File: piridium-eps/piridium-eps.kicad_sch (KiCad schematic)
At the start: 15 parts

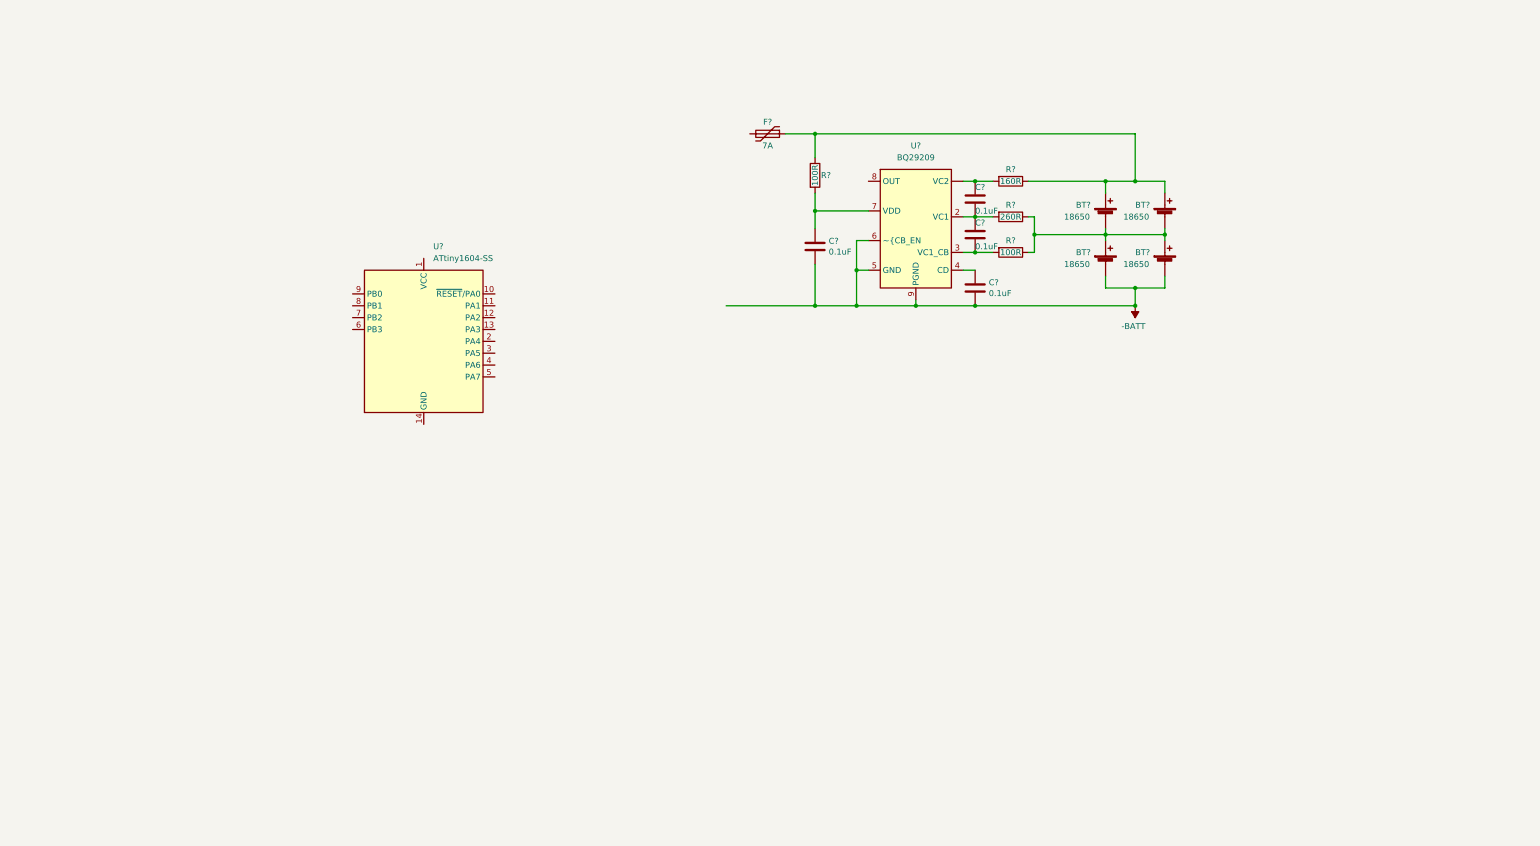
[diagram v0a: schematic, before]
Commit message: transfer some TJ-EPS circuitry to eps
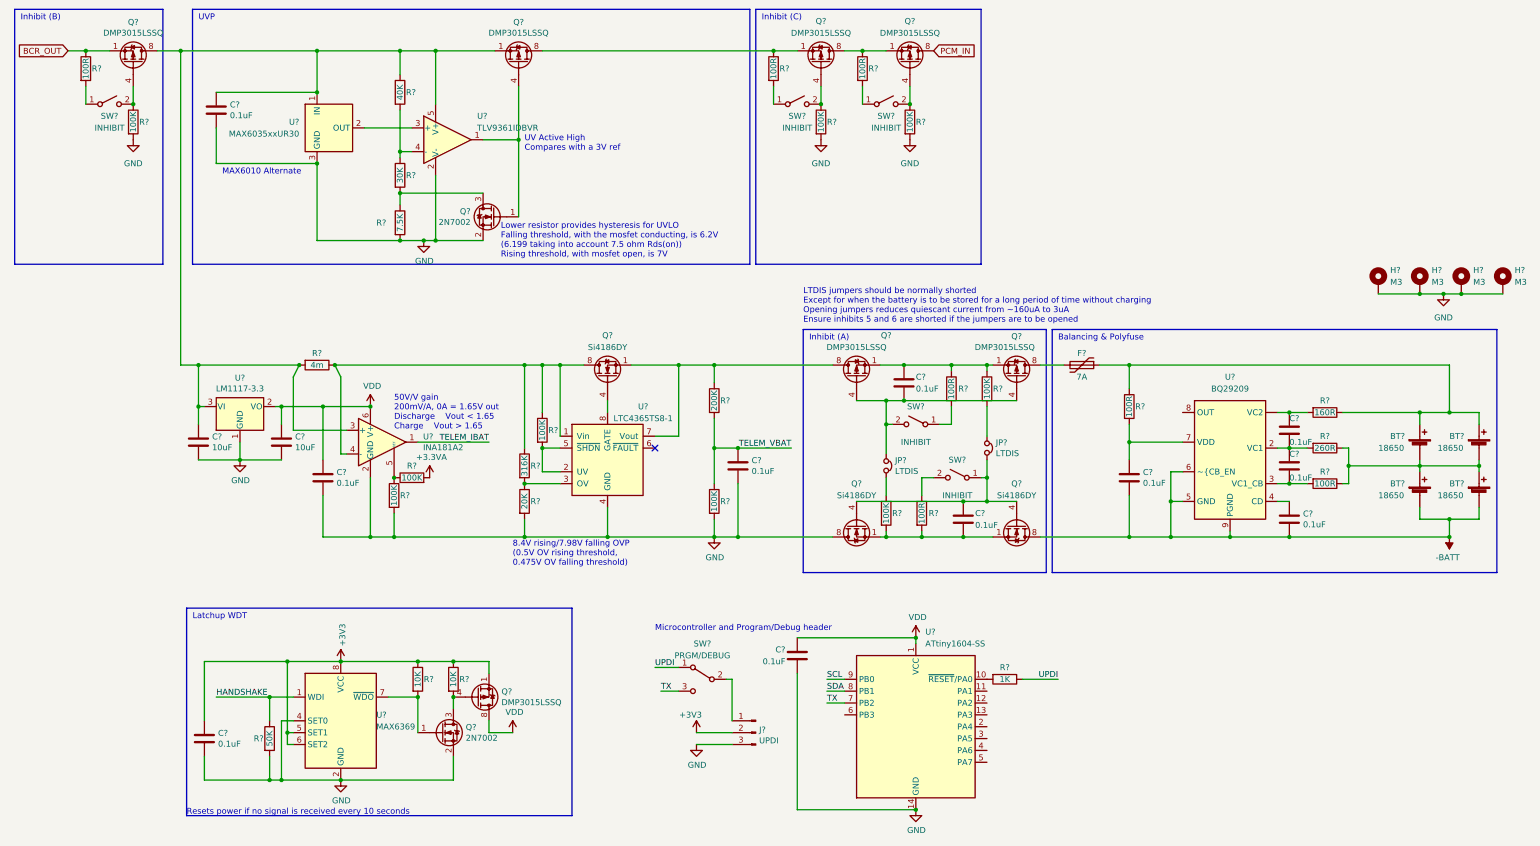
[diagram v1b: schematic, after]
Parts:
- added C? (x6): 0.1uF, Capacitor_SMD:C_0805_2012Metric, symbol Device:C
- added C? (x2): 10uF, Capacitor_SMD:C_0805_2012Metric, symbol Device:C
- added C?: 0.1uF, symbol Device:C
- added H? (x4): M3, MountingHole:MountingHole_3.2mm_M3_DIN965_Pad, symbol Mechanical:MountingHole_Pad
- added J?: UPDI, Connector_PinHeader_2.54mm:PinHeader_1x03_P2.54mm_Vertical, symbol Connector:Conn_01x03_Male
- added JP? (x2): LTDIS, Jumper:SolderJumper-2_P1.3mm_Open_Pad1.0x1.5mm, symbol BatteryMaster-rescue:Jumper_NC_Small-Device
- added Q? (x7): DMP3015LSSQ, Package_SO:SOIC-8_3.9x4.9mm_P1.27mm, symbol Transistor_FET:IRF7404
- added Q? (x2): 2N7002, Package_TO_SOT_SMD:SOT-23, symbol Transistor_FET:2N7002
- added Q? (x3): Si4186DY, Package_SO:SOIC-8_3.9x4.9mm_P1.27mm, symbol Transistor_FET:Si4162DY
- added R? (x9): 100K, Resistor_SMD:R_0805_2012Metric, symbol Device:R
- added R?: 1K, Resistor_SMD:R_1206_3216Metric, symbol Device:R
- added R? (x5): 100R, Resistor_SMD:R_0805_2012Metric, symbol Device:R
- added R?: 200K, Resistor_SMD:R_0805_2012Metric, symbol Device:R
- added R?: 30K, Resistor_SMD:R_0805_2012Metric, symbol Device:R
- added R? (x2): 10K, Resistor_SMD:R_0805_2012Metric, symbol Device:R
- added R?: 7.5K, Resistor_SMD:R_0805_2012Metric, symbol Device:R
- added R?: 4m, Resistor_SMD:R_1206_3216Metric, symbol Device:R
- added R?: 40K, Resistor_SMD:R_0805_2012Metric, symbol Device:R
- added R?: 316K, Resistor_SMD:R_0805_2012Metric, symbol Device:R
- added R?: 20K, Resistor_SMD:R_0805_2012Metric, symbol Device:R
- added R?: 50K, Resistor_SMD:R_0805_2012Metric, symbol Device:R
- added SW? (x5): INHIBIT, Connector_Hirose:Hirose_DF13-02P-1.25DSA_1x02_P1.25mm_Vertical, symbol Switch:SW_SPST
- added SW?: PRGM/DEBUG, Button_Switch_THT:SW_Slide_1P2T_CK_OS102011MS2Q, symbol Switch:SW_SPDT
- added U?: INA181A2, Package_TO_SOT_SMD:SOT-23-6, symbol Amplifier_Current:INA181
- added U?: MAX6369, Package_TO_SOT_SMD:SOT-23-8, symbol Power_Supervisor:MAX6369
- added U?: LM1117-3.3, Package_TO_SOT_SMD:SOT-223-3_TabPin2, symbol Regulator_Linear:LM1117-3.3
- added U?: LTC4365TS8-1, Package_TO_SOT_SMD:TSOT-23-8, symbol Power_Management:LTC4365TS8-1
- added U?: MAX6035xxUR30, Package_TO_SOT_SMD:SOT-23, symbol Reference_Voltage:MAX6035xxUR30
- added U?: TLV9361IDBVR, Package_TO_SOT_SMD:SOT-23-5, symbol Amplifier_Operational:OPA842xDBV
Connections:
- net -BATT: now also Q?.5 (D), Q?.6 (D), Q?.7 (D), Q?.8 (D)
- net at F?.2: now also Q?.5 (D), Q?.6 (D), Q?.7 (D), Q?.8 (D)
- net VDD: now reaches U?.1 (VCC)
- net VDD: now also C?.1, C?.1, C?.1, Q?.5 (D), Q?.6 (D), Q?.7 (D), Q?.8 (D), U?.2 (VO), U?.6 (V+)
- net at U?.10 (~{RESET}/PA0): now also R?.2
- net GND: now reaches U?.14 (GND)
- net GND: now also C?.2, C?.2, C?.2, C?.2, C?.2, C?.2, C?.2, H?.1, H?.1, H?.1, H?.1, J?.3 (Pin_3), Q?.2 (S), Q?.2 (S), Q?.5 (D), Q?.6 (D), Q?.7 (D), Q?.8 (D), R?.2, R?.2, R?.2, R?.2, R?.2, R?.2, R?.2, R?.2, U?.1 (GND), U?.2 (GND), U?.2 (GND), U?.2 (V-), U?.3 (GND), U?.4 (GND), U?.4 (SET0)
- net TX: now reaches U?.7 (PB2)
- net TX: now also SW?.3 (C)
- net SDA: now reaches U?.8 (PB1)
- net SCL: now reaches U?.9 (PB0)
- new net: Q?.4 (G), R?.1, SW?.2 (B) (x3)
- new net: C?.1, C?.1, Q?.1 (S), Q?.2 (S), Q?.3 (S), Q?.5 (D), Q?.6 (D), Q?.7 (D), Q?.8 (D), R?.1, R?.2, U?.1 (IN), U?.3 (+), U?.3 (VI), U?.5 (V+)
- new net: Q?.5 (D), Q?.6 (D), Q?.7 (D), Q?.8 (D), R?.1, R?.1, R?.1, U?.1 (Vin), U?.4 (-)
- new net: R?.1, R?.1, U?.5 (REF)
- new net: C?.1, Q?.1 (S), Q?.1 (S), Q?.2 (S), Q?.2 (S), Q?.3 (S), Q?.3 (S), R?.1, R?.1
- new net: R?.2, SW?.1 (A) (x4)
- new net: Q?.1 (S), Q?.2 (S), Q?.3 (S), Q?.5 (D), Q?.6 (D), Q?.7 (D), Q?.8 (D), R?.1, U?.7 (Vout)
- new net: Q?.1 (G), Q?.4 (G), U?.1
- new net: Q?.3 (D), R?.1, R?.2
- new net: C?.2, JP?.1, Q?.4 (G), Q?.4 (G), SW?.2 (B)
- new net: JP?.2, R?.1
- new net: R?.1, SW?.2 (B)
- new net: C?.2, Q?.1 (S), Q?.1 (S), Q?.2 (S), Q?.2 (S), Q?.3 (S), Q?.3 (S), R?.2, R?.2
- new net: C?.1, JP?.2, Q?.4 (G), Q?.4 (G), SW?.1 (A)
- new net: R?.1, R?.2, U?.4 (-)
- new net: J?.1 (Pin_1), SW?.2 (B)
- new net: Q?.1 (S), Q?.2 (S), Q?.3 (S), Q?.5 (D), Q?.6 (D), Q?.7 (D), Q?.8 (D), R?.1 (x2)
- new net: Q?.1 (G), R?.2, U?.7 (~{WDO})
- new net: Q?.3 (D), Q?.4 (G), R?.2
- new net: R?.2, U?.2 (UV), U?.5 (~{SHDN})
- new net: R?.1, R?.2, U?.3 (OV)
- new net: Q?.4 (G), U?.8 (GATE)
- new net: U?.2 (OUT), U?.3 (+)
- new net: JP?.1, R?.2
- new net +3.3VA: R?.2
- new net +3V3: C?.1, J?.2 (Pin_2), Q?.1 (S), Q?.2 (S), Q?.3 (S), R?.1, R?.1, U?.5 (SET1), U?.6 (SET2), U?.8 (VCC)
- new net BCR_OUT: Q?.1 (S), Q?.2 (S), Q?.3 (S), R?.1
- new net HANDSHAKE: R?.1, U?.1 (WDI)
- new net PCM_IN: Q?.5 (D), Q?.6 (D), Q?.7 (D), Q?.8 (D)
- new net TELEM_IBAT: U?.1
- new net TELEM_VBAT: C?.1, R?.1, R?.2
- new net UPDI: R?.1, SW?.1 (A)
- no-connect marks 0 -> 1
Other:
- note added: "50V/V gain 200mV/A, 0A = 1.65V out Discharge Vout < 1.65 Charge Vout > 1.65"
- note added: "8.4V rising/7.98V falling OVP (0.5V OV rising threshold, 0.475V OV falling threshold)"
- note added: "Balancing & Polyfuse"
- note added: "Inhibit (A)"
- note added: "Inhibit (B)"
- note added: "Inhibit (C)"
- note added: "LTDIS jumpers should be normally shorted Except for when the battery is to be stored for a long period of time without charging Opening jumpers reduces quiescant current from ~160uA to 3uA Ensure inhibits 5 and 6 are shorted if the jumpers are to be opened"
- note added: "Latchup WDT"
- note added: "Lower resistor provides hysteresis for UVLO Falling threshold, with the mosfet conducting, is 6.2V (6.199 taking into account 7.5 ohm Rds(on)) Rising threshold, with mosfet open, is 7V"
- note added: "MAX6010 Alternate"
- note added: "Microcontroller and Program/Debug header"
- note added: "Resets power if no signal is received every 10 seconds"
- note added: "UV Active High Compares with a 3V ref"
- note added: "UVP"
- moved on the sheet: BT?, C?, F?, R?, U?

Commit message: fix bus board messup, remove redundant components from eps
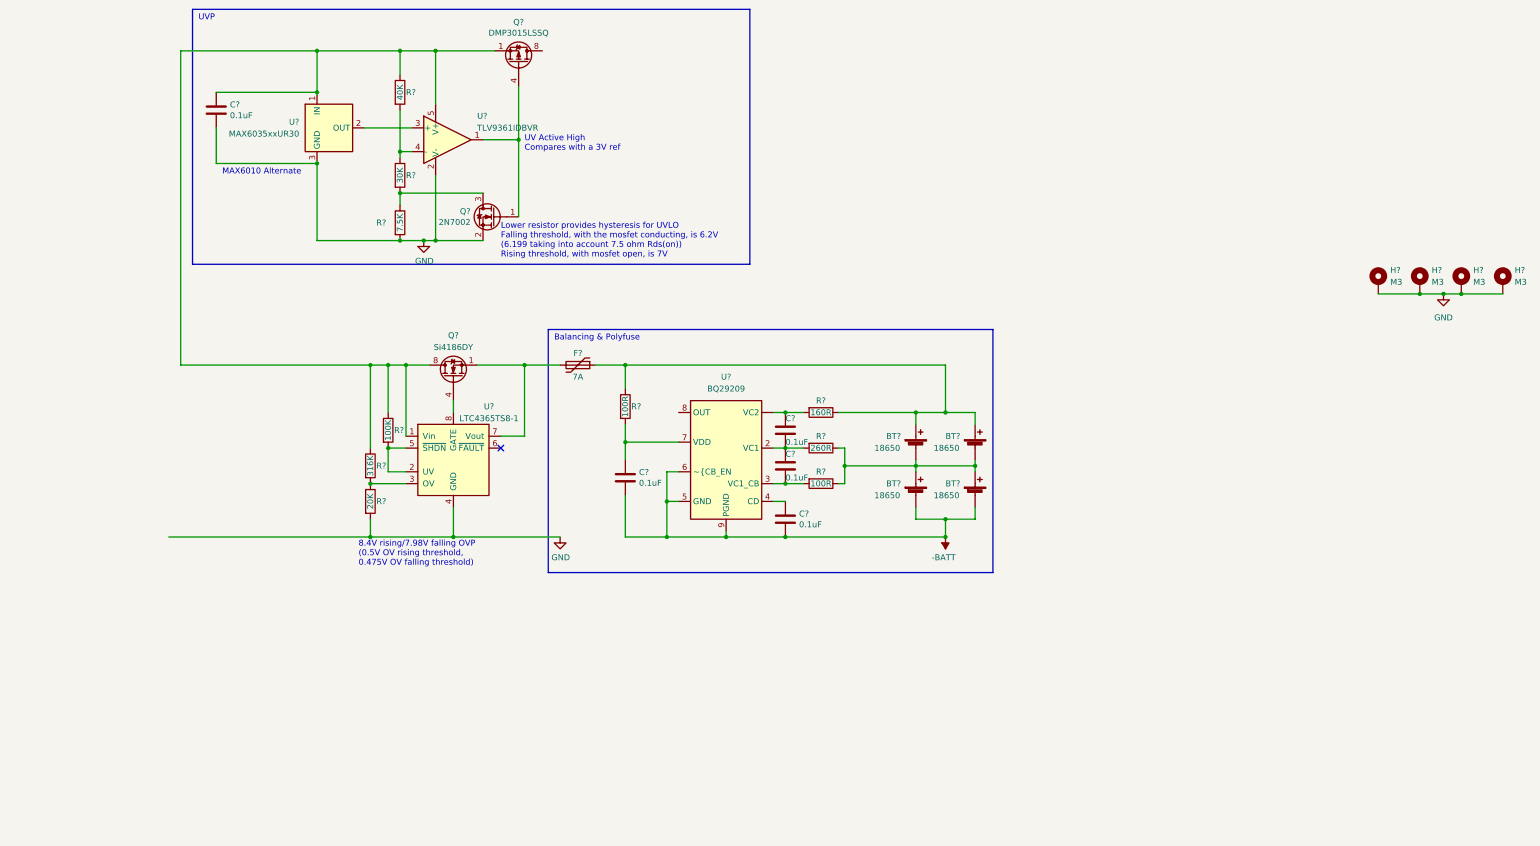
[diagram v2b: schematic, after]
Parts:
- removed C? (x5): 0.1uF, Capacitor_SMD:C_0805_2012Metric, symbol Device:C
- removed C? (x2): 10uF, Capacitor_SMD:C_0805_2012Metric, symbol Device:C
- removed C?: 0.1uF, symbol Device:C
- removed J?: UPDI, Connector_PinHeader_2.54mm:PinHeader_1x03_P2.54mm_Vertical, symbol Connector:Conn_01x03_Male
- removed JP? (x2): LTDIS, Jumper:SolderJumper-2_P1.3mm_Open_Pad1.0x1.5mm, symbol BatteryMaster-rescue:Jumper_NC_Small-Device
- removed Q? (x6): DMP3015LSSQ, Package_SO:SOIC-8_3.9x4.9mm_P1.27mm, symbol Transistor_FET:IRF7404
- removed Q? (x2): Si4186DY, Package_SO:SOIC-8_3.9x4.9mm_P1.27mm, symbol Transistor_FET:Si4162DY
- removed Q?: 2N7002, Package_TO_SOT_SMD:SOT-23, symbol Transistor_FET:2N7002
- removed R? (x8): 100K, Resistor_SMD:R_0805_2012Metric, symbol Device:R
- removed R?: 1K, Resistor_SMD:R_1206_3216Metric, symbol Device:R
- removed R? (x5): 100R, Resistor_SMD:R_0805_2012Metric, symbol Device:R
- removed R?: 200K, Resistor_SMD:R_0805_2012Metric, symbol Device:R
- removed R? (x2): 10K, Resistor_SMD:R_0805_2012Metric, symbol Device:R
- removed R?: 4m, Resistor_SMD:R_1206_3216Metric, symbol Device:R
- removed R?: 50K, Resistor_SMD:R_0805_2012Metric, symbol Device:R
- removed SW? (x5): INHIBIT, Connector_Hirose:Hirose_DF13-02P-1.25DSA_1x02_P1.25mm_Vertical, symbol Switch:SW_SPST
- removed SW?: PRGM/DEBUG, Button_Switch_THT:SW_Slide_1P2T_CK_OS102011MS2Q, symbol Switch:SW_SPDT
- removed U?: INA181A2, Package_TO_SOT_SMD:SOT-23-6, symbol Amplifier_Current:INA181
- removed U?: MAX6369, Package_TO_SOT_SMD:SOT-23-8, symbol Power_Supervisor:MAX6369
- removed U?: LM1117-3.3, Package_TO_SOT_SMD:SOT-223-3_TabPin2, symbol Regulator_Linear:LM1117-3.3
- removed U?: ATtiny1604-SS, Package_SO:SOIC-14_3.9x8.7mm_P1.27mm, symbol MCU_Microchip_ATtiny:ATtiny1604-SS
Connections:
- net at C?.1, Q?.1 (S), Q?.2 (S)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: now also Q?.5 (D), Q?.6 (D), Q?.7 (D), Q?.8 (D), R?.1, R?.1, U?.1 (Vin)
- net at Q?.1 (S), Q?.2 (S), Q?.3 (S)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: now also F?.2
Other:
- note removed: "50V/V gain 200mV/A, 0A = 1.65V out Discharge Vout < 1.65 Charge Vout > 1.65"
- note removed: "Inhibit (A)"
- note removed: "Inhibit (B)"
- note removed: "Inhibit (C)"
- note removed: "LTDIS jumpers should be normally shorted Except for when the battery is to be stored for a long period of time without charging Opening jumpers reduces quiescant current from ~160uA to 3uA Ensure inhibits 5 and 6 are shorted if the jumpers are to be opened"
- note removed: "Latchup WDT"
- note removed: "Microcontroller and Program/Debug header"
- note removed: "Resets power if no signal is received every 10 seconds"
- moved on the sheet: BT?, C?, F?, Q?, R?, U?

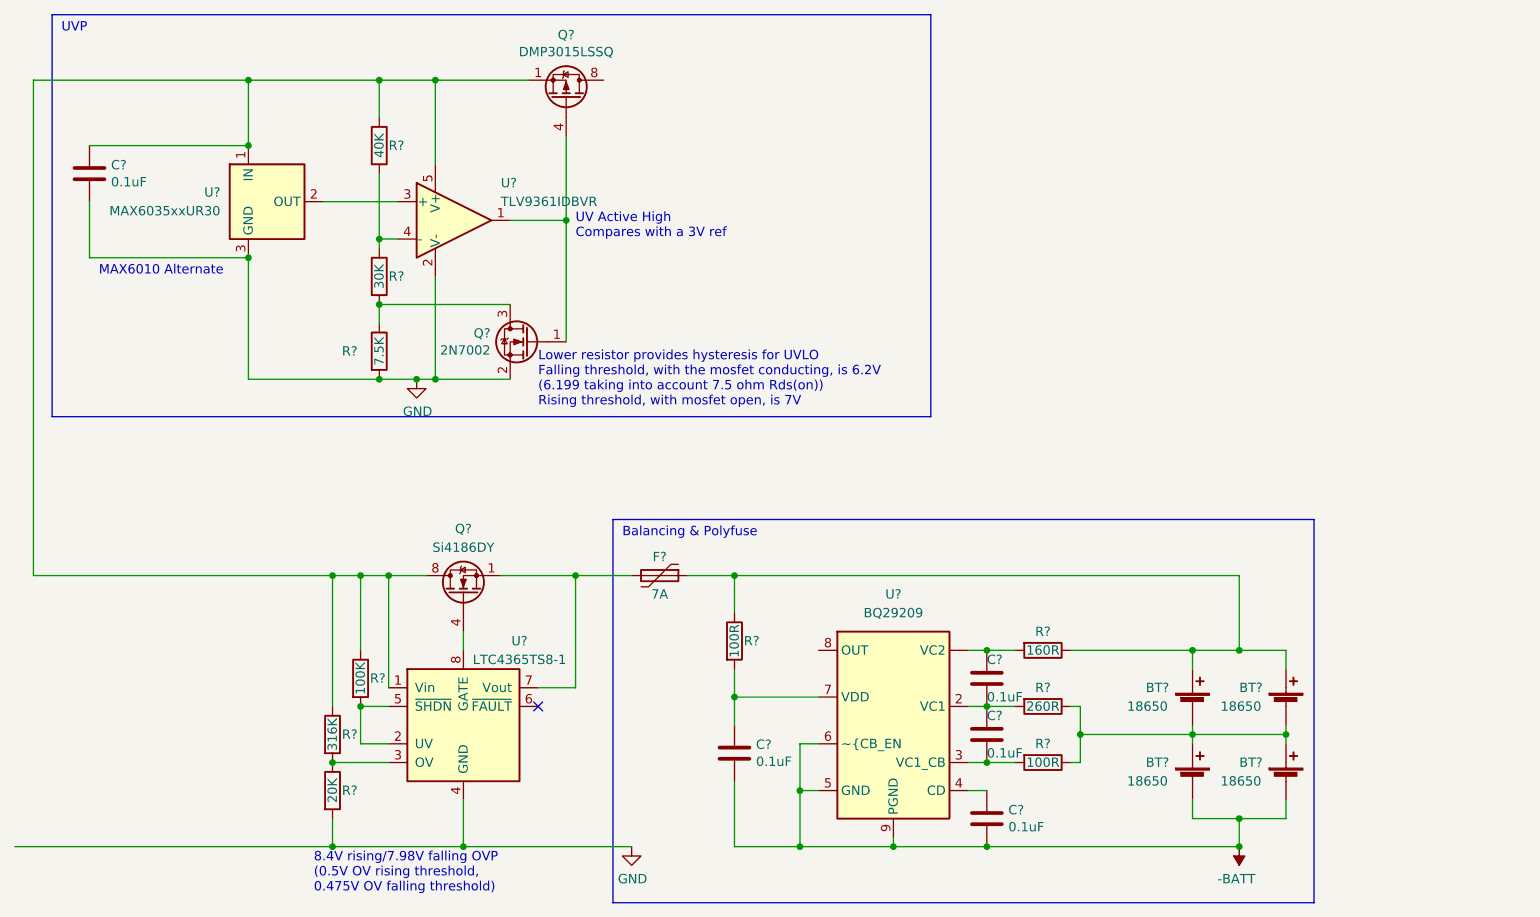
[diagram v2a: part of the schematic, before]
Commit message: copy pycubed battery
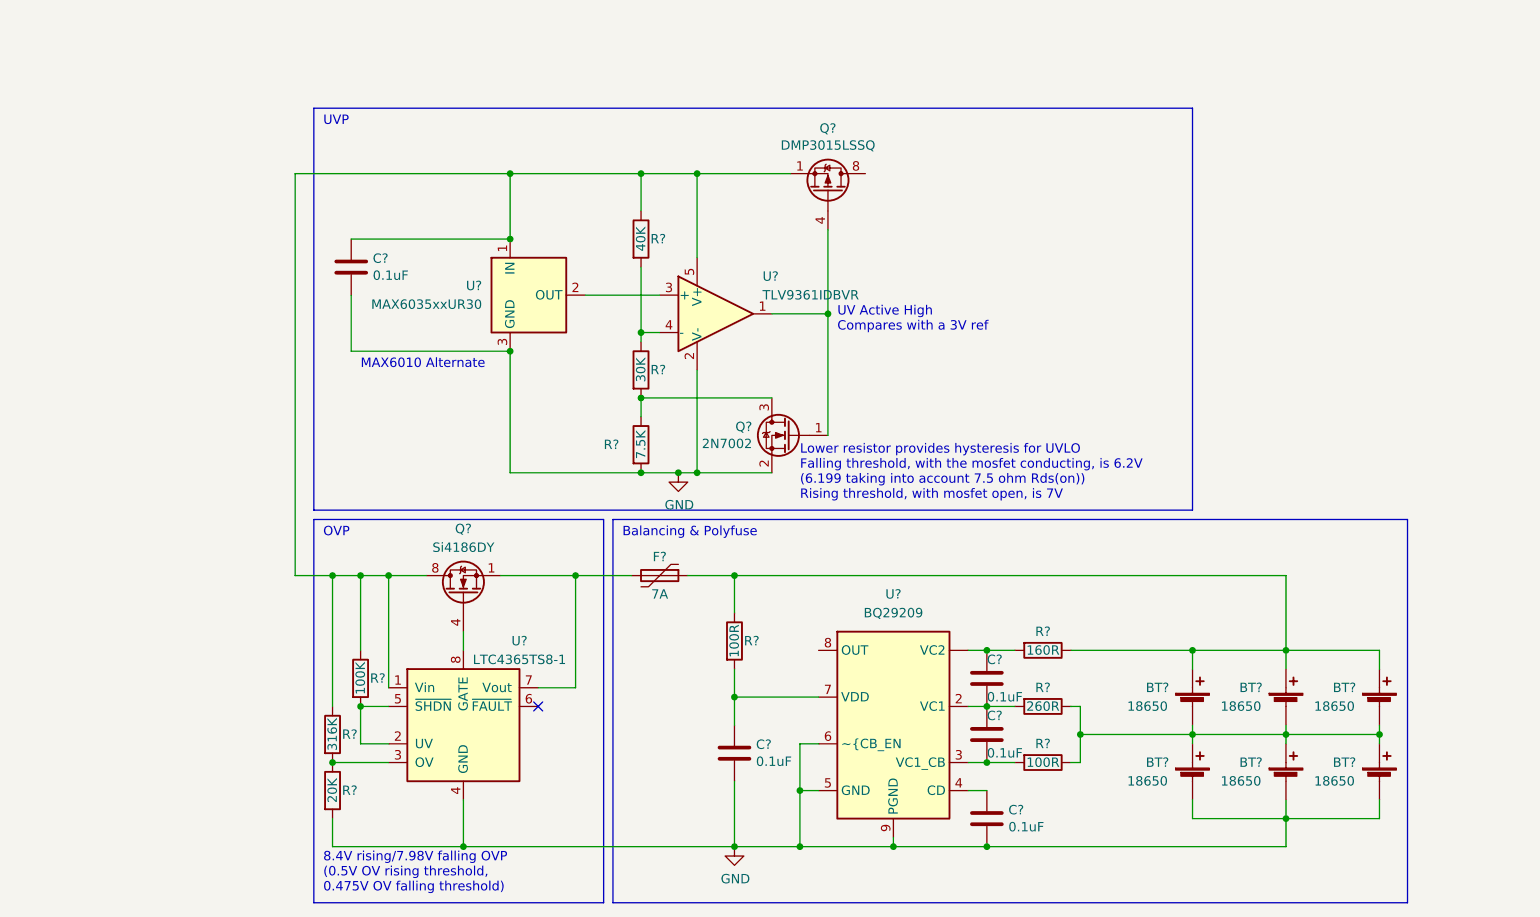
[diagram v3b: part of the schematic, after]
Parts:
- added BT? (x2): 18650, piridium-eps:18650-weld, symbol Device:Battery_Cell
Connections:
- net -BATT is gone; now on net GND: BT?.2 (-), BT?.2 (-), C?.2, C?.2, U?.5 (GND), U?.6 (~{CB_EN), U?.9 (PGND)
- net GND: now also BT?.2 (-)
- net at BT?.1 (+), BT?.1 (+), BT?.2 (-)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: now also BT?.1 (+), BT?.2 (-)
- net at BT?.1 (+), BT?.1 (+), F?.1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: now also BT?.1 (+)
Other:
- note added: "OVP"
- moved on the sheet: C?, Q?, R?, U?
